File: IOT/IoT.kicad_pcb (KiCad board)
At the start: 2 copper layers, 140.9 x 93.7 mm, 147 parts, among them IC1 MAX3222EAP+, IC2 MAX3222EAP+, J1 USB_C_Receptacle_USB2.0_16P, J10 Program header, J11 Conn_01x08_Pin, J12 Micro_SD_Card_Det2, J13 Conn_01x08_Pin, J14 Flow sensor, J15 RS232_1, J16 RS232_1, J17 24V, J18 12V, J19 5V, J2 Conn_01x20_Pin, J20 3V3, J21 heated blanket, J3 Conn_01x04_Pin, J4 Conn_01x04_Pin, Q1 AO3400A, SW1 SW_Push, SW2 SW_Push, SW3 SW_Push, SW4 SW_Push, SW5 SW_Push, U1 STM32F401RETx, U2 TPS5430DDA, U3 TPS5430DDA, U4 MCP73831-3-OT, U5 TPS61040DBVR, U6 AMS1117-3.3, Y1 16MHz, Y2 32.768khz

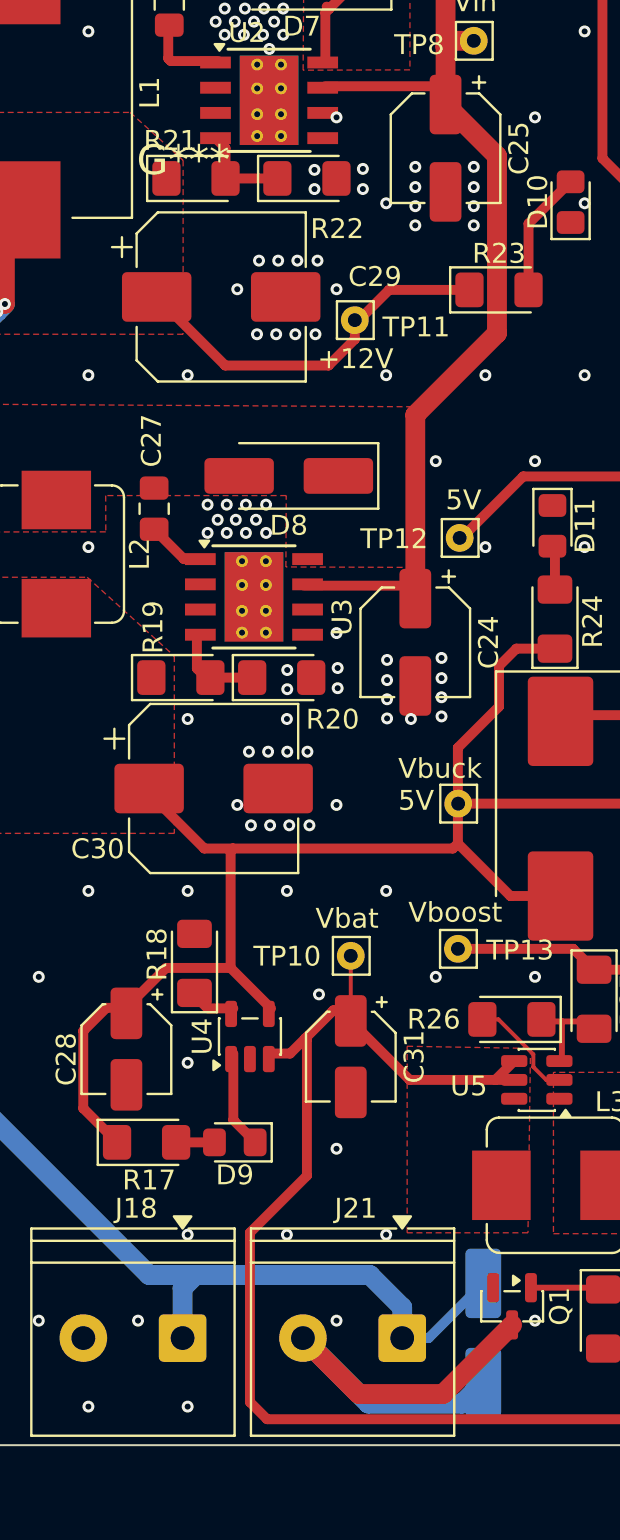
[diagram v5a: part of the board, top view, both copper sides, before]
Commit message: checked DRC and generated gerber files
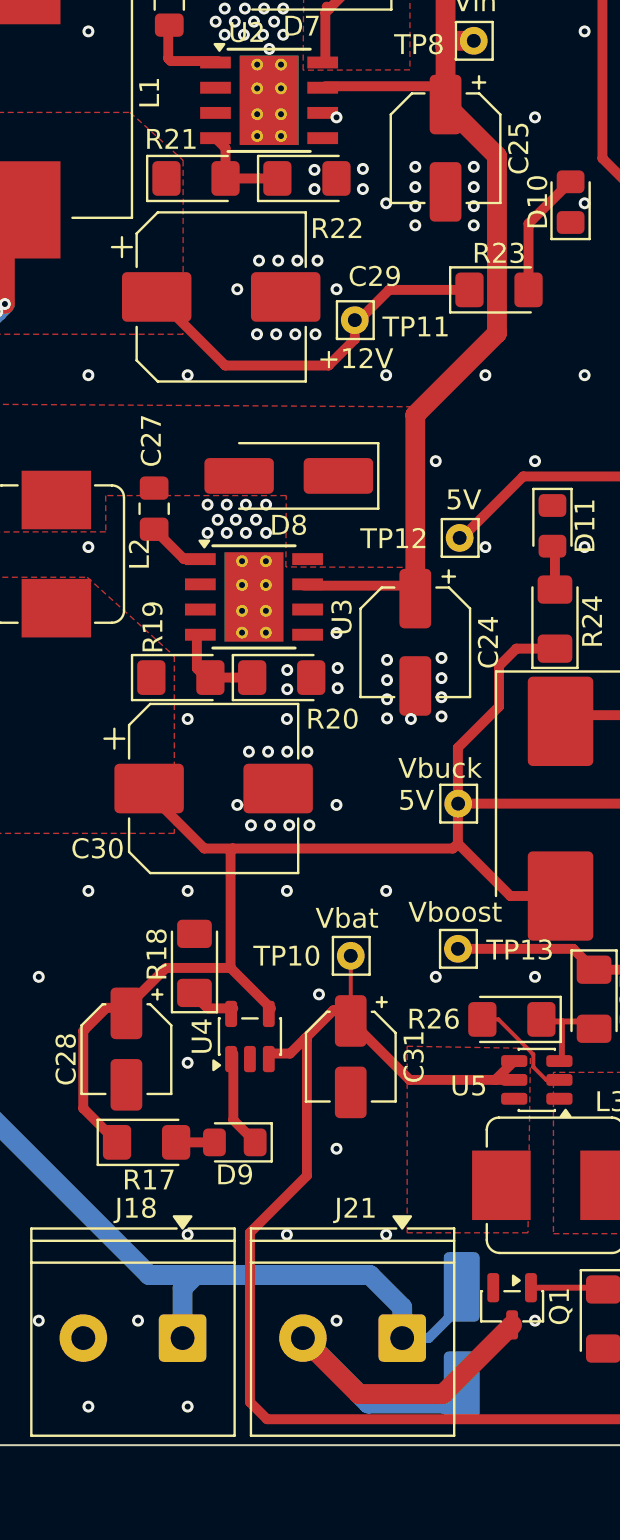
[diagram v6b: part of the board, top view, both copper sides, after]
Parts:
- moved D22 1.10 mm to (93.0, 135.2)
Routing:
- net Net-(D22-A): track 24.0 -> 22.9 mm
- net +12V: track 104.1 -> 103.4 mm
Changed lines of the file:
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@@
 		(capping no)
 		(filling no)
+		(zone_defaults)
 		(pcbplotparams
 			(layerselection 0x00000000_00000000_55555555_5755f5ff)
@@
 		(tags "LED handsolder")
 		(property "Reference" "R21"
-			(at -1.2954 -1.905 0)
+			(at -1.2446 -1.9558 0)
 			(layer "F.SilkS")
 			(effects
@@
 		(at 78.98 75.921 180)
 		(property "Reference" "G***"
-			(at 0 0 0)
+			(at 14.5656 -7.7466 0)
 			(layer "F.SilkS")
+			(hide yes)
 			(effects
 				(font
@@
 	(footprint "Diode_SMD:D_SMA_Handsoldering"
 		(layer "B.Cu")
-		(at 94.104 134.999 -90)
+		(at 93.0148 135.1788 -90)
 		(descr "Diode SMA (DO-214AC) Handsoldering")
 		(tags "Diode SMA (DO-214AC) Handsoldering")
@@
 	)
 	(segment
+		(start 93.0148 133.5882)
+		(end 91.3473 135.2557)
+		(width 0.5)
+		(layer "B.Cu")
+		(net "+12V")
+	)
+	(segment
 		(start 77.2668 132.08)
 		(end 64.7192 119.5324)
@@
 	)
 	(segment
-		(start 94.104 132.499)
-		(end 91.3473 135.2557)
-		(width 0.5)
-		(layer "B.Cu")
-		(net "+12V")
-	)
-	(segment
 		(start 79.6036 132.08)
 		(end 77.2668 132.08)
@@
 	)
 	(segment
+		(start 93.0148 132.6788)
+		(end 93.0148 133.5882)
+		(width 0.5)
+		(layer "B.Cu")
+		(net "+12V")
+	)
+	(segment
 		(start 90.0176 135.2557)
 		(end 90.0176 133.7056)
@@
 	)
 	(segment
+		(start 91.3473 135.2557)
+		(end 90.0176 135.2557)
+		(width 0.5)
+		(layer "B.Cu")
+		(net "+12V")
+	)
+	(segment
 		(start 90.0176 133.7056)
 		(end 88.392 132.08)
@@
 	)
 	(segment
-		(start 91.3473 135.2557)
-		(end 90.0176 135.2557)
-		(width 0.5)
-		(layer "B.Cu")
-		(net "+12V")
-	)
-	(segment
 		(start 64.7192 88.4428)
 		(end 69.1896 83.9724)
@@
 	)
 	(segment
+		(start 87.8363 138.0744)
+		(end 85.0176 135.2557)
+		(width 1)
+		(layer "F.Cu")
+		(net "Net-(D22-A)")
+	)
+	(segment
+		(start 95.5548 134.5923)
+		(end 92.0727 138.0744)
+		(width 1)
+		(layer "F.Cu")
+		(net "Net-(D22-A)")
+	)
+	(segment
+		(start 92.0727 138.0744)
+		(end 87.8363 138.0744)
+		(width 1)
+		(layer "F.Cu")
+		(net "Net-(D22-A)")
+	)
+	(segment
+		(start 85.0176 135.2557)
+		(end 88.3189 138.557)
+		(width 1)
+		(layer "B.Cu")
+		(net "Net-(D22-A)")
+	)
+	(segment
+		(start 92.1366 138.557)
+		(end 93.0148 137.6788)
+		(width 1)
+		(layer "B.Cu")
+		(net "Net-(D22-A)")
+	)
+	(segment
+		(start 88.3189 138.557)
+		(end 92.1366 138.557)
+		(width 1)
+		(layer "B.Cu")
+		(net "Net-(D22-A)")
+	)
+	(segment
 		(start 148.9456 97.6376)
 		(end 149.4536 97.6376)
@@
 		(net "/PC13")
 	)
-	(segment
-		(start 87.8363 138.0744)
-		(end 85.0176 135.2557)
-		(width 1)
-		(layer "F.Cu")
-		(net "Net-(D22-A)")
-	)
-	(segment
-		(start 95.5548 134.5923)
-		(end 92.0727 138.0744)
-		(width 1)
-		(layer "F.Cu")
-		(net "Net-(D22-A)")
-	)
-	(segment
-		(start 92.0727 138.0744)
-		(end 87.8363 138.0744)
-		(width 1)
-		(layer "F.Cu")
-		(net "Net-(D22-A)")
-	)
-	(segment
-		(start 93.046 138.557)
-		(end 94.104 137.499)
-		(width 1)
-		(layer "B.Cu")
-		(net "Net-(D22-A)")
-	)
-	(segment
-		(start 85.0176 135.2557)
-		(end 88.3189 138.557)
-		(width 1)
-		(layer "B.Cu")
-		(net "Net-(D22-A)")
-	)
-	(segment
-		(start 88.3189 138.557)
-		(end 93.046 138.557)
-		(width 1)
-		(layer "B.Cu")
-		(net "Net-(D22-A)")
-	)
 	(zone
